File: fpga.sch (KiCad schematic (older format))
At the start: 2 parts

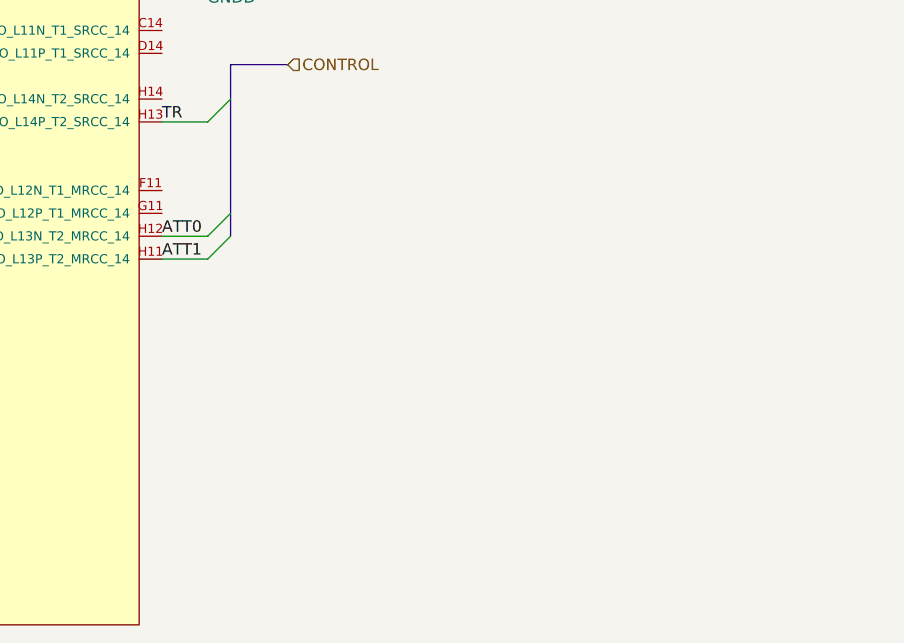
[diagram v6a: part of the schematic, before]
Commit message: Add oscillator
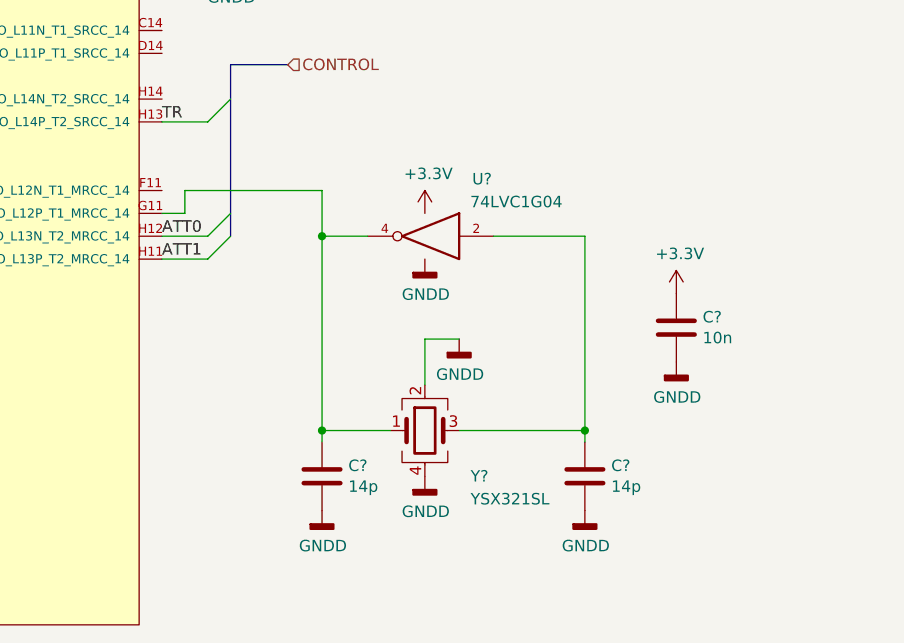
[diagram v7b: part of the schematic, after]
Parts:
- added C?: 10n, symbol Device:C
- added C? (x2): 14p, symbol Device:C
- added U?: 74LVC1G04, symbol 74xGxx:74LVC1G04
- added Y?: YSX321SL, Crystal:Crystal_SMD_3225-4Pin_3.2x2.5mm, symbol Device:Crystal_GND24
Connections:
- net +3V3: now also C?.1, U?.5 (VCC)
- net at U?.G11 (IO_L12P_T1_MRCC_14): now also C?.1, U?.4, Y?.1
- net GNDD renamed GND
- net GND: now also C?.2, C?.2, C?.2, U?.3 (GND), Y?.2, Y?.4
- new net: C?.1, U?.2, Y?.3
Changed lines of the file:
@@
 Wire Wire Line
 	4100 1700 4100 1600
-Wire Bus Line
-	8250 3650 8250 4400
-Wire Bus Line
-	3650 4700 3650 6000
-Wire Bus Line
-	3650 2250 3650 4600
 $Comp
 L Device:R R?
@@
 Text Notes 8350 3250 0    50   ~ 0
 FPGA Internal Pull-up states for Select IO pins during configuration
+$Comp
+L 74xGxx:74LVC1G04 U?
+U 1 1 609D4D51
+P 9100 4400
+F 0 "U?" H 8850 4650 50  0000 C CNN
+F 1 "74LVC1G04" H 8700 4550 50  0000 C CNN
+F 2 "" H 9100 4400 50  0001 C CNN
+F 3 "http://www.ti.com/lit/sg/scyt129e/scyt129e.pdf" H 9100 4400 50  0001 C CNN
+	1    9100 4400
+	-1   0    0    -1
+$EndComp
+$Comp
+L power:GNDD #PWR?
+U 1 1 609D7C96
+P 9100 4500
+F 0 "#PWR?" H 9100 4250 50  0001 C CNN
+F 1 "GNDD" H 9104 4345 50  0000 C CNN
+F 2 "" H 9100 4500 50  0001 C CNN
+F 3 "" H 9100 4500 50  0001 C CNN
+	1    9100 4500
+	1    0    0    -1
+$EndComp
+$Comp
+L power:+3.3V #PWR?
+U 1 1 609D8B52
+P 9100 4300
+F 0 "#PWR?" H 9100 4150 50  0001 C CNN
+F 1 "+3.3V" H 9115 4473 50  0000 C CNN
+F 2 "" H 9100 4300 50  0001 C CNN
+F 3 "" H 9100 4300 50  0001 C CNN
+	1    9100 4300
+	1    0    0    -1
+$EndComp
+$Comp
+L power:+3.3V #PWR?
+U 1 1 609D9246
+P 10200 4650
+F 0 "#PWR?" H 10200 4500 50  0001 C CNN
+F 1 "+3.3V" H 10215 4823 50  0000 C CNN
+F 2 "" H 10200 4650 50  0001 C CNN
+F 3 "" H 10200 4650 50  0001 C CNN
+	1    10200 4650
+	1    0    0    -1
+$EndComp
+$Comp
+L power:GNDD #PWR?
+U 1 1 609D99F2
+P 10200 4950
+F 0 "#PWR?" H 10200 4700 50  0001 C CNN
+F 1 "GNDD" H 10204 4795 50  0000 C CNN
+F 2 "" H 10200 4950 50  0001 C CNN
+F 3 "" H 10200 4950 50  0001 C CNN
+	1    10200 4950
+	1    0    0    -1
+$EndComp
+$Comp
+L Device:C C?
+U 1 1 609DA11F
+P 10200 4800
+F 0 "C?" H 10315 4846 50  0000 L CNN
+F 1 "10n" H 10315 4755 50  0000 L CNN
+F 2 "" H 10238 4650 50  0001 C CNN
+F 3 "~" H 10200 4800 50  0001 C CNN
+	1    10200 4800
+	1    0    0    -1
+$EndComp
+$Comp
+L Device:Crystal_GND24 Y?
+U 1 1 609DB3A4
+P 9100 5250
+F 0 "Y?" H 9300 5050 50  0000 L CNN
+F 1 "YSX321SL" H 9300 4950 50  0000 L CNN
+F 2 "Crystal:Crystal_SMD_3225-4Pin_3.2x2.5mm" H 9100 5250 50  0001 C CNN
+F 3 "https://datasheet.lcsc.com/lcsc/2103291203_Yangxing-Tech-X322525MOB4SI_C9006.pdf" H 9100 5250 50  0001 C CNN
+	1    9100 5250
+	1    0    0    -1
+$EndComp
+$Comp
+L power:GNDD #PWR?
+U 1 1 609DC8C0
+P 9250 4850
+F 0 "#PWR?" H 9250 4600 50  0001 C CNN
+F 1 "GNDD" H 9254 4695 50  0000 C CNN
+F 2 "" H 9250 4850 50  0001 C CNN
+F 3 "" H 9250 4850 50  0001 C CNN
+	1    9250 4850
+	1    0    0    -1
+$EndComp
+Wire Wire Line
+	9250 4850 9100 4850
+Wire Wire Line
+	9100 4850 9100 5050
+$Comp
+L power:GNDD #PWR?
+U 1 1 609DDDB8
+P 9100 5450
+F 0 "#PWR?" H 9100 5200 50  0001 C CNN
+F 1 "GNDD" H 9104 5295 50  0000 C CNN
+F 2 "" H 9100 5450 50  0001 C CNN
+F 3 "" H 9100 5450 50  0001 C CNN
+	1    9100 5450
+	1    0    0    -1
+$EndComp
+$Comp
+L Device:C C?
+U 1 1 609DE8CE
+P 9800 5450
+F 0 "C?" H 9915 5496 50  0000 L CNN
+F 1 "14p" H 9915 5405 50  0000 L CNN
+F 2 "" H 9838 5300 50  0001 C CNN
+F 3 "~" H 9800 5450 50  0001 C CNN
+	1    9800 5450
+	1    0    0    -1
+$EndComp
+$Comp
+L Device:C C?
+U 1 1 609DEF0A
+P 8650 5450
+F 0 "C?" H 8765 5496 50  0000 L CNN
+F 1 "14p" H 8765 5405 50  0000 L CNN
+F 2 "" H 8688 5300 50  0001 C CNN
+F 3 "~" H 8650 5450 50  0001 C CNN
+	1    8650 5450
+	1    0    0    -1
+$EndComp
+$Comp
+L power:GNDD #PWR?
+U 1 1 609DF822
+P 8650 5600
+F 0 "#PWR?" H 8650 5350 50  0001 C CNN
+F 1 "GNDD" H 8654 5445 50  0000 C CNN
+F 2 "" H 8650 5600 50  0001 C CNN
+F 3 "" H 8650 5600 50  0001 C CNN
+	1    8650 5600
+	1    0    0    -1
+$EndComp
+$Comp
+L power:GNDD #PWR?
+U 1 1 609DFC05
+P 9800 5600
+F 0 "#PWR?" H 9800 5350 50  0001 C CNN
+F 1 "GNDD" H 9804 5445 50  0000 C CNN
+F 2 "" H 9800 5600 50  0001 C CNN
+F 3 "" H 9800 5600 50  0001 C CNN
+	1    9800 5600
+	1    0    0    -1
+$EndComp
+Wire Wire Line
+	9250 5250 9800 5250
+Wire Wire Line
+	9800 5250 9800 5300
+Wire Wire Line
+	8950 5250 8650 5250
+Wire Wire Line
+	8650 5250 8650 5300
+Wire Wire Line
+	8850 4400 8650 4400
+Wire Wire Line
+	8650 4400 8650 5250
+Connection ~ 8650 5250
+Wire Wire Line
+	9400 4400 9800 4400
+Wire Wire Line
+	9800 4400 9800 5250
+Connection ~ 9800 5250
+Wire Wire Line
+	7950 4300 8050 4300
+Wire Wire Line
+	8050 4300 8050 4200
+Wire Wire Line
+	8050 4200 8650 4200
+Wire Wire Line
+	8650 4200 8650 4400
+Connection ~ 8650 4400
+Wire Bus Line
+	8250 3650 8250 4400
+Wire Bus Line
+	3650 4700 3650 6000
+Wire Bus Line
+	3650 2250 3650 4600
 $EndSCHEMATC

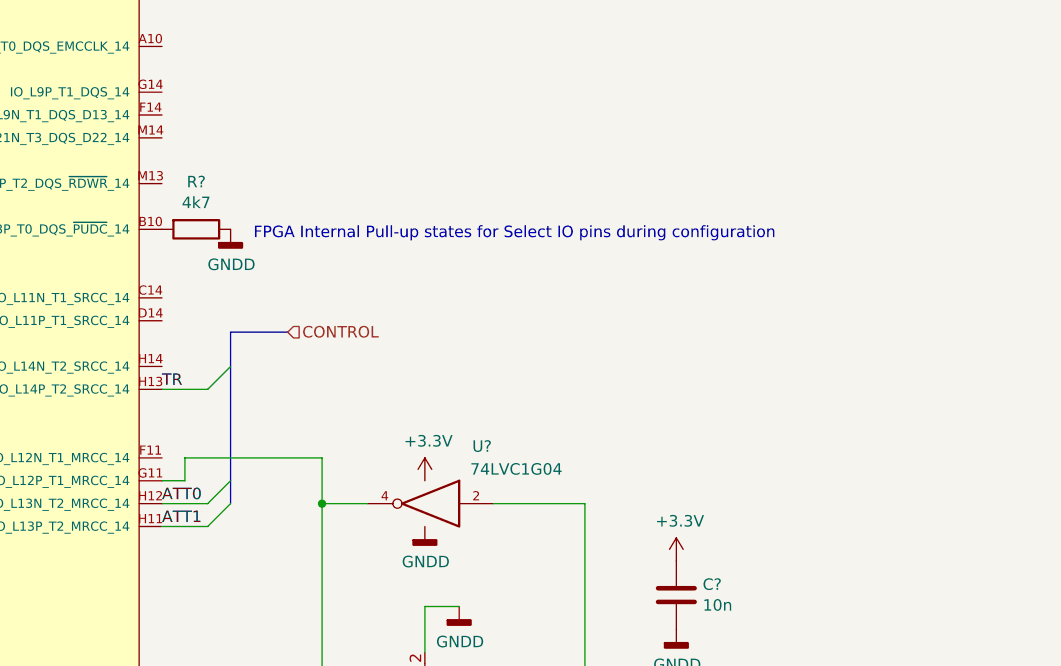
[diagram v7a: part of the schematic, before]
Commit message: Connect USB buses to the FPGA
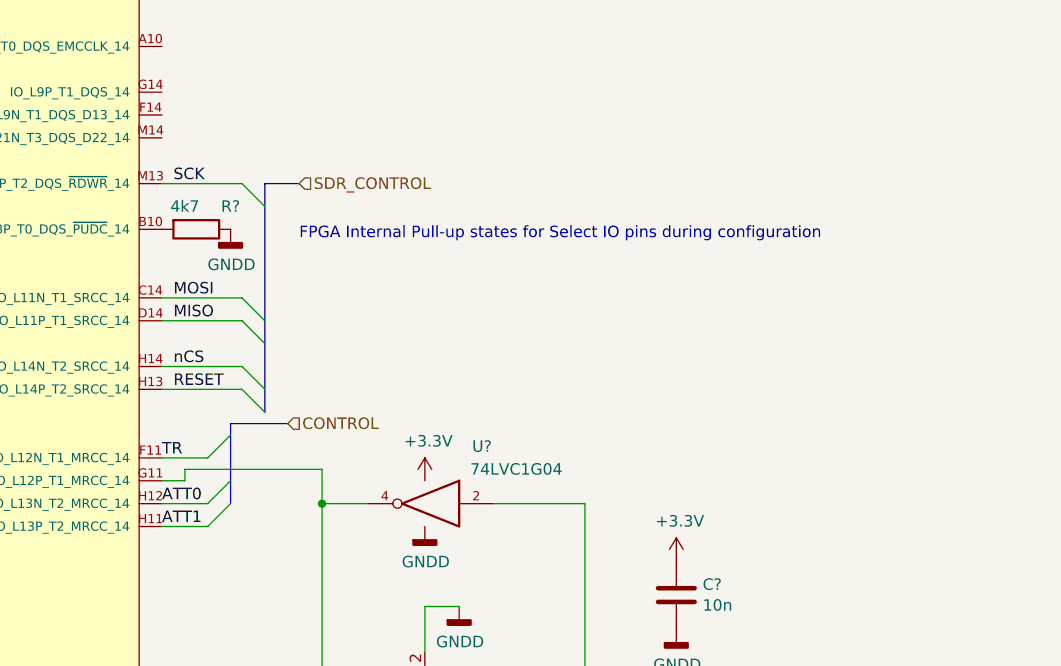
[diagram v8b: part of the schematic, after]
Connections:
- net TR: now also U?.F11 (IO_L12N_T1_MRCC_14); no longer U?.H13 (IO_L14P_T2_SRCC_14)
- net MOSI: now reaches U?.C14 (IO_L11N_T1_SRCC_14)
- net MISO: now reaches U?.D14 (IO_L11P_T1_SRCC_14)
- net nCS: now reaches U?.H14 (IO_L14N_T2_SRCC_14)
- net SCK: now reaches U?.M13 (IO_L15P_T2_DQS_~RDWR~_14)
- new net RESET: U?.H13 (IO_L14P_T2_SRCC_14)
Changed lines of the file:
@@
 Text Label 7950 4500 0    50   ~ 0
 ATT1
-Text Label 7950 3900 0    50   ~ 0
+Text Label 7950 4200 0    50   ~ 0
 TR
 Wire Bus Line
-	8250 3650 8500 3650
-Text HLabel 8500 3650 2    50   Input ~ 0
+	8250 4050 8500 4050
+Text HLabel 8500 4050 2    50   Input ~ 0
 CONTROL
 Entry Wire Line
-	8150 3900 8250 3800
+	8150 4200 8250 4100
 Entry Wire Line
 	8150 4500 8250 4400
@@
 	7950 4500 8150 4500
 Wire Wire Line
-	8150 3900 7950 3900
+	8150 4200 7950 4200
 Wire Wire Line
 	3750 4600 4250 4600
@@
 U 1 1 609B728D
 P 8100 3200
-F 0 "R?" V 7893 3200 50  0000 C CNN
-F 1 "4k7" V 7984 3200 50  0000 C CNN
+F 0 "R?" V 8000 3350 50  0000 C CNN
+F 1 "4k7" V 8000 3150 50  0000 C CNN
 F 2 "" V 8030 3200 50  0001 C CNN
 F 3 "~" H 8100 3200 50  0001 C CNN
@@
 	1    0    0    -1
 $EndComp
-Text Notes 8350 3250 0    50   ~ 0
+Text Notes 8550 3250 0    50   ~ 0
 FPGA Internal Pull-up states for Select IO pins during configuration
 $Comp
@@
 	7950 4300 8050 4300
 Wire Wire Line
-	8050 4300 8050 4200
-Wire Wire Line
-	8050 4200 8650 4200
-Wire Wire Line
-	8650 4200 8650 4400
+	8050 4300 8050 4250
+Wire Wire Line
+	8050 4250 8650 4250
+Wire Wire Line
+	8650 4250 8650 4400
 Connection ~ 8650 4400
-Wire Bus Line
-	8250 3650 8250 4400
+Entry Wire Line
+	8300 3500 8400 3600
+Entry Wire Line
+	8300 3600 8400 3700
+Entry Wire Line
+	8300 3000 8400 3100
+Entry Wire Line
+	8300 3800 8400 3900
+Text Label 8000 3500 0    50   ~ 0
+MOSI
+Text Label 8000 3600 0    50   ~ 0
+MISO
+Text Label 8000 3000 0    50   ~ 0
+SCK
+Text Label 8000 3800 0    50   ~ 0
+nCS
+Wire Bus Line
+	8400 3000 8550 3000
+Text HLabel 8550 3000 2    50   Input ~ 0
+SDR_CONTROL
+Wire Wire Line
+	7950 3500 8300 3500
+Wire Wire Line
+	7950 3600 8300 3600
+Wire Wire Line
+	7950 3000 8300 3000
+Wire Wire Line
+	7950 3800 8300 3800
+Wire Wire Line
+	7950 3900 8300 3900
+Text Label 8000 3900 0    50   ~ 0
+RESET
+Entry Wire Line
+	8300 3900 8400 4000
+Wire Bus Line
+	8250 4050 8250 4400
+Wire Bus Line
+	8400 3000 8400 4000
 Wire Bus Line
 	3650 4700 3650 6000
